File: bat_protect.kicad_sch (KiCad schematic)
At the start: 16 parts

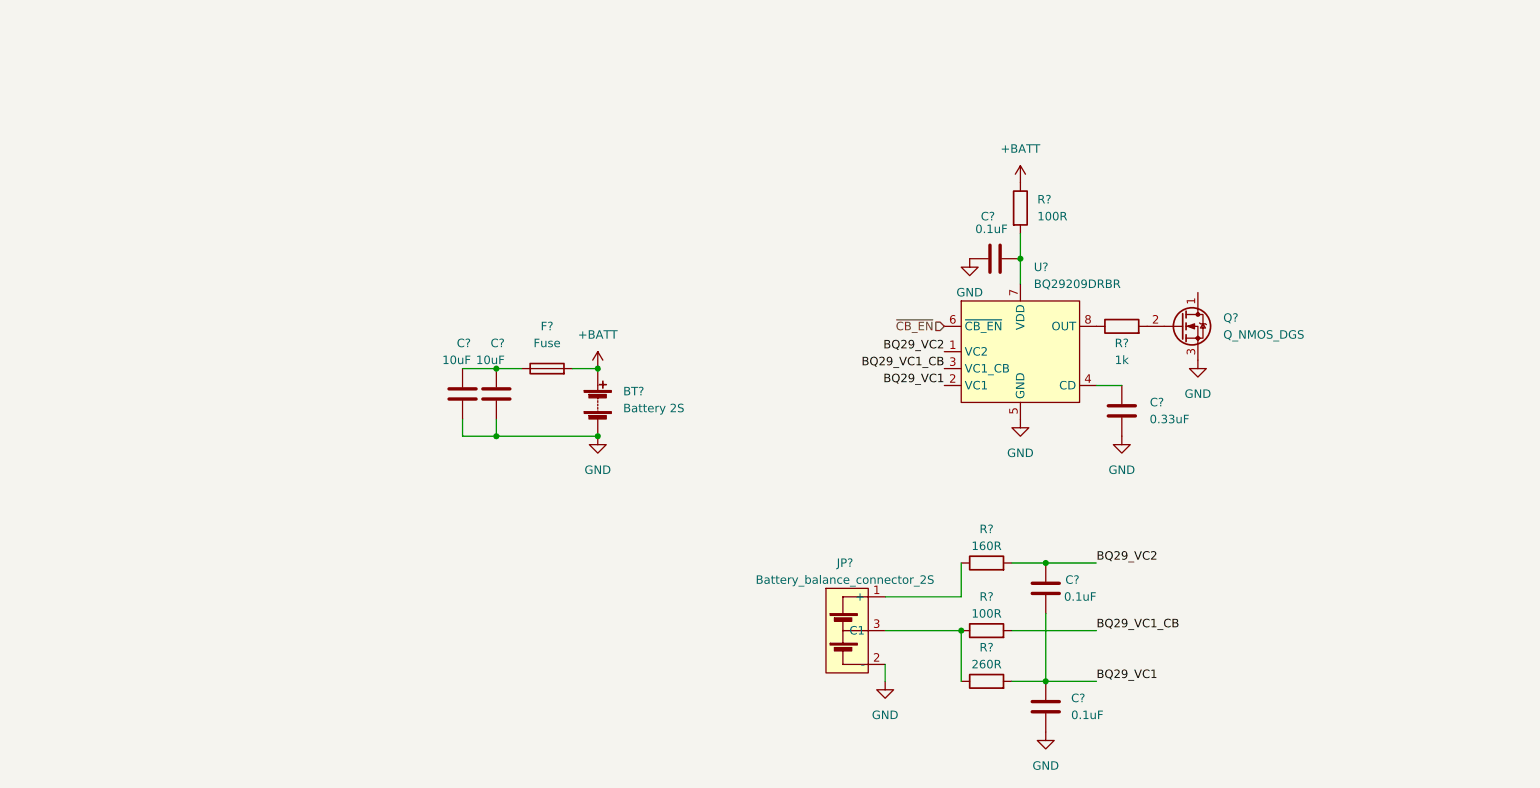
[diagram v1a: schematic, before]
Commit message: added audio ref schematic, added bat to 5V, added shift register, connected devices with other periferals
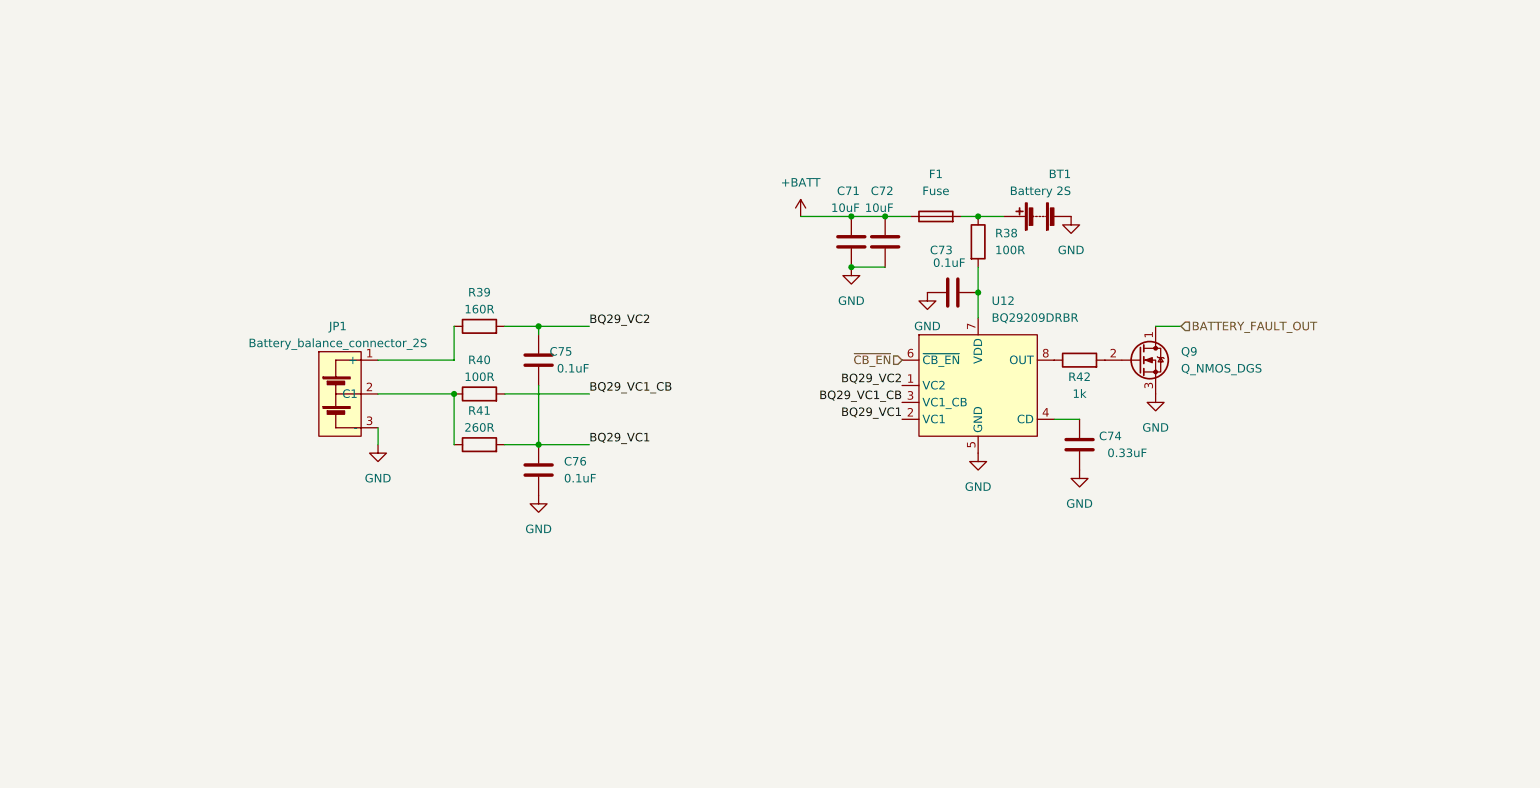
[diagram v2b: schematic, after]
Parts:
- gave numbers to parts that had none: 16
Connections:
- net +BATT: now also C71.2, C72.2, F1.1; no longer BT1.1 (+), F1.2, R38.1
- net GND: now also JP1.3 (-); no longer JP1.2 (-)
- net at R40.1, R41.1: now also JP1.2 (C1); no longer JP1.3 (C1)
- net BATTERY_FAULT_OUT: now reaches Q9.1 (D)
- new net: BT1.1 (+), F1.2, R38.1
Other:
- moved on the sheet: BT1, C71, C72, C73, C74, C75, C76, F1, JP1, Q9, R38, R39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

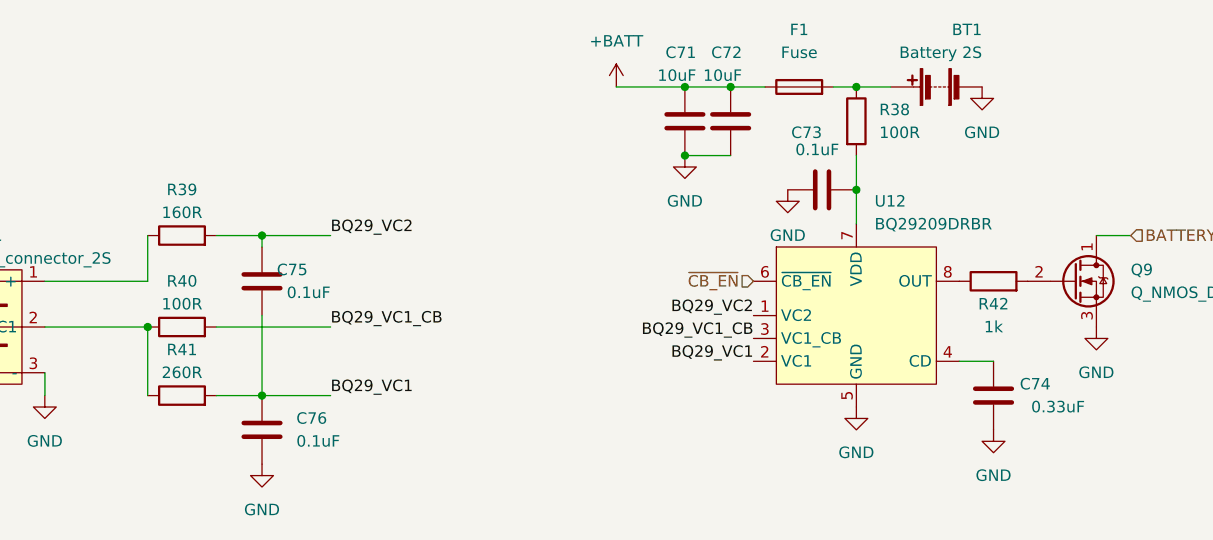
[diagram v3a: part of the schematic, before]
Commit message: minor optimized pinassignement, added capacitors, added connectors
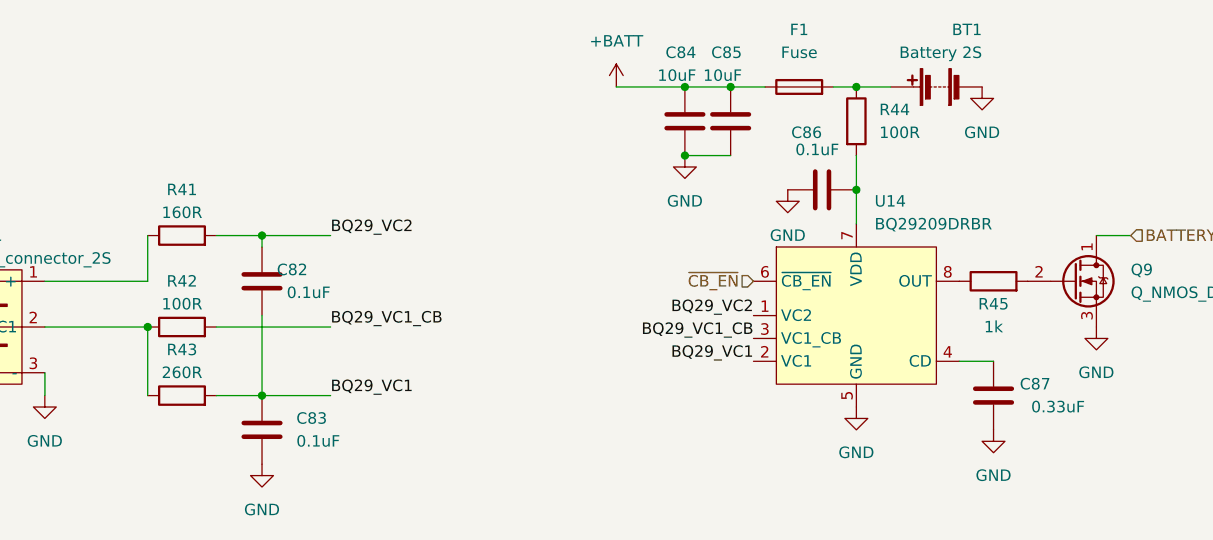
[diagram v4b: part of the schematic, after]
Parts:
- renumbered C75 to C82, C76 to C83, C71 to C84, C72 to C85, C73 to C86, C74 to C87, R39 to R41, R40 to R42, R41 to R43, R38 to R44, R42 to R45, U12 to U14
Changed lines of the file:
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@@
   (symbol (lib_id "power:GND") (at 78.74 99.06 0) (unit 1)
     (in_bom yes) (on_board yes) (fields_autoplaced)
-    (property "Reference" "#PWR0198" (id 0) (at 78.74 105.41 0)
+    (property "Reference" "#PWR0110" (id 0) (at 78.74 105.41 0)
       (effects (font (size 1.27 1.27)) hide)
     )
@@
   (symbol (lib_id "Device:R") (at 93.98 91.44 90) (unit 1)
     (in_bom yes) (on_board yes)
-    (property "Reference" "R40" (id 0) (at 93.98 86.36 90))
+    (property "Reference" "R42" (id 0) (at 93.98 86.36 90))
     (property "Value" "100R" (id 1) (at 93.98 88.9 90))
     (property "Footprint" "" (id 2) (at 93.98 93.218 90)
@@
   (symbol (lib_id "power:+BATT") (at 142.24 64.77 0) (unit 1)
     (in_bom yes) (on_board yes) (fields_autoplaced)
-    (property "Reference" "#PWR0193" (id 0) (at 142.24 68.58 0)
+    (property "Reference" "#PWR0112" (id 0) (at 142.24 68.58 0)
       (effects (font (size 1.27 1.27)) hide)
     )
@@
   (symbol (lib_id "power:GND") (at 102.87 106.68 0) (unit 1)
     (in_bom yes) (on_board yes) (fields_autoplaced)
-    (property "Reference" "#PWR0197" (id 0) (at 102.87 113.03 0)
+    (property "Reference" "#PWR0111" (id 0) (at 102.87 113.03 0)
       (effects (font (size 1.27 1.27)) hide)
     )
@@
   (symbol (lib_id "power:GND") (at 168.91 100.33 0) (unit 1)
     (in_bom yes) (on_board yes) (fields_autoplaced)
-    (property "Reference" "#PWR0191" (id 0) (at 168.91 106.68 0)
+    (property "Reference" "#PWR0115" (id 0) (at 168.91 106.68 0)
       (effects (font (size 1.27 1.27)) hide)
     )
@@
   (symbol (lib_id "power:GND") (at 149.86 72.39 0) (unit 1)
     (in_bom yes) (on_board yes) (fields_autoplaced)
-    (property "Reference" "#PWR0190" (id 0) (at 149.86 78.74 0)
+    (property "Reference" "#PWR0113" (id 0) (at 149.86 78.74 0)
       (effects (font (size 1.27 1.27)) hide)
     )
@@
   (symbol (lib_id "power:GND") (at 182.88 64.77 0) (unit 1)
     (in_bom yes) (on_board yes) (fields_autoplaced)
-    (property "Reference" "#PWR0242" (id 0) (at 182.88 71.12 0)
+    (property "Reference" "#PWR0116" (id 0) (at 182.88 71.12 0)
       (effects (font (size 1.27 1.27)) hide)
     )
@@
   (symbol (lib_id "Device:R") (at 93.98 81.28 90) (unit 1)
     (in_bom yes) (on_board yes)
-    (property "Reference" "R39" (id 0) (at 93.98 76.2 90))
+    (property "Reference" "R41" (id 0) (at 93.98 76.2 90))
     (property "Value" "160R" (id 1) (at 93.98 78.74 90))
     (property "Footprint" "" (id 2) (at 93.98 83.058 90)
@@
   (symbol (lib_id "power:GND") (at 161.29 76.2 0) (unit 1)
     (in_bom yes) (on_board yes) (fields_autoplaced)
-    (property "Reference" "#PWR0192" (id 0) (at 161.29 82.55 0)
+    (property "Reference" "#PWR0114" (id 0) (at 161.29 82.55 0)
       (effects (font (size 1.27 1.27)) hide)
     )
@@
   (symbol (lib_id "Device:C") (at 184.15 99.06 0) (mirror x) (unit 1)
     (in_bom yes) (on_board yes)
-    (property "Reference" "C74" (id 0) (at 190.5 97.79 0)
+    (property "Reference" "C87" (id 0) (at 190.5 97.79 0)
       (effects (font (size 1.27 1.27)) (justify right))
     )
@@
   (symbol (lib_id "Device:R") (at 184.15 86.36 90) (unit 1)
     (in_bom yes) (on_board yes)
-    (property "Reference" "R42" (id 0) (at 184.15 88.9 90))
+    (property "Reference" "R45" (id 0) (at 184.15 88.9 90))
     (property "Value" "1k" (id 1) (at 184.15 91.44 90))
     (property "Footprint" "" (id 2) (at 184.15 88.138 90)
@@
   (symbol (lib_id "Device:C") (at 102.87 102.87 0) (mirror y) (unit 1)
     (in_bom yes) (on_board yes)
-    (property "Reference" "C76" (id 0) (at 106.68 101.6 0)
+    (property "Reference" "C83" (id 0) (at 106.68 101.6 0)
       (effects (font (size 1.27 1.27)) (justify right))
     )
@@
   (symbol (lib_id "power:GND") (at 195.58 91.44 0) (unit 1)
     (in_bom yes) (on_board yes) (fields_autoplaced)
-    (property "Reference" "#PWR0195" (id 0) (at 195.58 97.79 0)
+    (property "Reference" "#PWR0118" (id 0) (at 195.58 97.79 0)
       (effects (font (size 1.27 1.27)) hide)
     )
@@
   (symbol (lib_id "power:GND") (at 184.15 102.87 0) (unit 1)
     (in_bom yes) (on_board yes) (fields_autoplaced)
-    (property "Reference" "#PWR0196" (id 0) (at 184.15 109.22 0)
+    (property "Reference" "#PWR0117" (id 0) (at 184.15 109.22 0)
       (effects (font (size 1.27 1.27)) hide)
     )
@@
   (symbol (lib_id "Device:C") (at 149.86 68.58 0) (mirror x) (unit 1)
     (in_bom yes) (on_board yes)
-    (property "Reference" "C71" (id 0) (at 151.13 60.96 0)
+    (property "Reference" "C84" (id 0) (at 151.13 60.96 0)
       (effects (font (size 1.27 1.27)) (justify right))
     )
@@
   (symbol (lib_id "Device:C") (at 154.94 68.58 0) (mirror x) (unit 1)
     (in_bom yes) (on_board yes)
-    (property "Reference" "C72" (id 0) (at 156.21 60.96 0)
+    (property "Reference" "C85" (id 0) (at 156.21 60.96 0)
       (effects (font (size 1.27 1.27)) (justify right))
     )
@@
   (symbol (lib_id "Device:C") (at 165.1 76.2 270) (mirror x) (unit 1)
     (in_bom yes) (on_board yes)
-    (property "Reference" "C73" (id 0) (at 165.1 69.85 90)
+    (property "Reference" "C86" (id 0) (at 165.1 69.85 90)
       (effects (font (size 1.27 1.27)) (justify right))
     )
@@
   (symbol (lib_id "Device:C") (at 102.87 86.36 0) (mirror x) (unit 1)
     (in_bom yes) (on_board yes)
-    (property "Reference" "C75" (id 0) (at 107.95 85.09 0)
+    (property "Reference" "C82" (id 0) (at 107.95 85.09 0)
       (effects (font (size 1.27 1.27)) (justify right))
     )
@@
   (symbol (lib_id "Device:R") (at 93.98 99.06 90) (unit 1)
     (in_bom yes) (on_board yes)
-    (property "Reference" "R41" (id 0) (at 93.98 93.98 90))
+    (property "Reference" "R43" (id 0) (at 93.98 93.98 90))
     (property "Value" "260R" (id 1) (at 93.98 96.52 90))
     (property "Footprint" "" (id 2) (at 93.98 100.838 90)
@@
   (symbol (lib_id "Device:R") (at 168.91 68.58 0) (unit 1)
     (in_bom yes) (on_board yes) (fields_autoplaced)
-    (property "Reference" "R38" (id 0) (at 171.45 67.3099 0)
+    (property "Reference" "R44" (id 0) (at 171.45 67.3099 0)
       (effects (font (size 1.27 1.27)) (justify left))
     )
@@
   (symbol (lib_id "airsoft_controller:BQ29209DRBR") (at 168.91 90.17 0) (unit 1)
     (in_bom yes) (on_board yes) (fields_autoplaced)
-    (property "Reference" "U12" (id 0) (at 170.9294 77.47 0)
-      (effects (font (size 1.27 1.27)) (justify left))
-    )
+    (property "Reference" "U14" (id 0) (at 170.9294 77.47 0)
+      (effects (font (size 1.27 1.27)) (justify left))
+    )

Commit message: PI LC lowpass filter, added CP2012 reset, added connectors
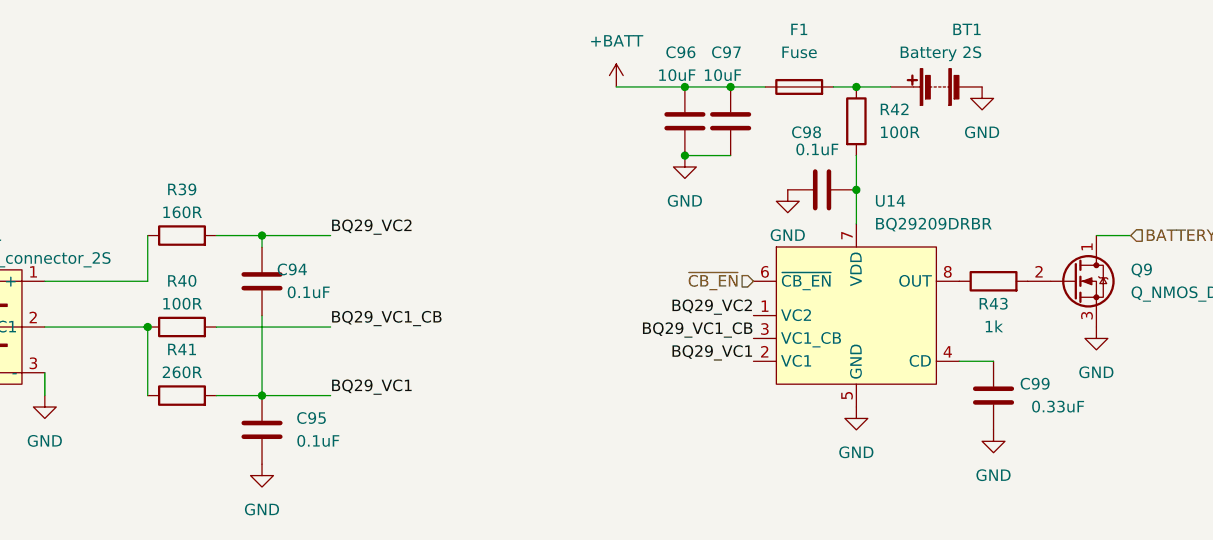
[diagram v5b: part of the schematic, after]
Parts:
- renumbered C82 to C94, C83 to C95, C84 to C96, C85 to C97, C86 to C98, C87 to C99, R41 to R39, R42 to R40, R43 to R41, R44 to R42, R45 to R43
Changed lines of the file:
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@@
   (symbol (lib_id "power:GND") (at 78.74 99.06 0) (unit 1)
     (in_bom yes) (on_board yes) (fields_autoplaced)
-    (property "Reference" "#PWR0110" (id 0) (at 78.74 105.41 0)
+    (property "Reference" "#PWR0117" (id 0) (at 78.74 105.41 0)
       (effects (font (size 1.27 1.27)) hide)
     )
@@
   (symbol (lib_id "Device:R") (at 93.98 91.44 90) (unit 1)
     (in_bom yes) (on_board yes)
-    (property "Reference" "R42" (id 0) (at 93.98 86.36 90))
+    (property "Reference" "R40" (id 0) (at 93.98 86.36 90))
     (property "Value" "100R" (id 1) (at 93.98 88.9 90))
     (property "Footprint" "" (id 2) (at 93.98 93.218 90)
@@
   (symbol (lib_id "power:+BATT") (at 142.24 64.77 0) (unit 1)
     (in_bom yes) (on_board yes) (fields_autoplaced)
-    (property "Reference" "#PWR0112" (id 0) (at 142.24 68.58 0)
+    (property "Reference" "#PWR0119" (id 0) (at 142.24 68.58 0)
       (effects (font (size 1.27 1.27)) hide)
     )
@@
   (symbol (lib_id "power:GND") (at 102.87 106.68 0) (unit 1)
     (in_bom yes) (on_board yes) (fields_autoplaced)
-    (property "Reference" "#PWR0111" (id 0) (at 102.87 113.03 0)
+    (property "Reference" "#PWR0118" (id 0) (at 102.87 113.03 0)
       (effects (font (size 1.27 1.27)) hide)
     )
@@
   (symbol (lib_id "power:GND") (at 168.91 100.33 0) (unit 1)
     (in_bom yes) (on_board yes) (fields_autoplaced)
-    (property "Reference" "#PWR0115" (id 0) (at 168.91 106.68 0)
+    (property "Reference" "#PWR0122" (id 0) (at 168.91 106.68 0)
       (effects (font (size 1.27 1.27)) hide)
     )
@@
   (symbol (lib_id "power:GND") (at 149.86 72.39 0) (unit 1)
     (in_bom yes) (on_board yes) (fields_autoplaced)
-    (property "Reference" "#PWR0113" (id 0) (at 149.86 78.74 0)
+    (property "Reference" "#PWR0120" (id 0) (at 149.86 78.74 0)
       (effects (font (size 1.27 1.27)) hide)
     )
@@
   (symbol (lib_id "power:GND") (at 182.88 64.77 0) (unit 1)
     (in_bom yes) (on_board yes) (fields_autoplaced)
-    (property "Reference" "#PWR0116" (id 0) (at 182.88 71.12 0)
+    (property "Reference" "#PWR0123" (id 0) (at 182.88 71.12 0)
       (effects (font (size 1.27 1.27)) hide)
     )
@@
   (symbol (lib_id "Device:R") (at 93.98 81.28 90) (unit 1)
     (in_bom yes) (on_board yes)
-    (property "Reference" "R41" (id 0) (at 93.98 76.2 90))
+    (property "Reference" "R39" (id 0) (at 93.98 76.2 90))
     (property "Value" "160R" (id 1) (at 93.98 78.74 90))
     (property "Footprint" "" (id 2) (at 93.98 83.058 90)
@@
   (symbol (lib_id "power:GND") (at 161.29 76.2 0) (unit 1)
     (in_bom yes) (on_board yes) (fields_autoplaced)
-    (property "Reference" "#PWR0114" (id 0) (at 161.29 82.55 0)
+    (property "Reference" "#PWR0121" (id 0) (at 161.29 82.55 0)
       (effects (font (size 1.27 1.27)) hide)
     )
@@
   (symbol (lib_id "Device:C") (at 184.15 99.06 0) (mirror x) (unit 1)
     (in_bom yes) (on_board yes)
-    (property "Reference" "C87" (id 0) (at 190.5 97.79 0)
+    (property "Reference" "C99" (id 0) (at 190.5 97.79 0)
       (effects (font (size 1.27 1.27)) (justify right))
     )
@@
   (symbol (lib_id "Device:R") (at 184.15 86.36 90) (unit 1)
     (in_bom yes) (on_board yes)
-    (property "Reference" "R45" (id 0) (at 184.15 88.9 90))
+    (property "Reference" "R43" (id 0) (at 184.15 88.9 90))
     (property "Value" "1k" (id 1) (at 184.15 91.44 90))
     (property "Footprint" "" (id 2) (at 184.15 88.138 90)
@@
   (symbol (lib_id "Device:C") (at 102.87 102.87 0) (mirror y) (unit 1)
     (in_bom yes) (on_board yes)
-    (property "Reference" "C83" (id 0) (at 106.68 101.6 0)
+    (property "Reference" "C95" (id 0) (at 106.68 101.6 0)
       (effects (font (size 1.27 1.27)) (justify right))
     )
@@
   (symbol (lib_id "power:GND") (at 195.58 91.44 0) (unit 1)
     (in_bom yes) (on_board yes) (fields_autoplaced)
-    (property "Reference" "#PWR0118" (id 0) (at 195.58 97.79 0)
+    (property "Reference" "#PWR0125" (id 0) (at 195.58 97.79 0)
       (effects (font (size 1.27 1.27)) hide)
     )
@@
   (symbol (lib_id "power:GND") (at 184.15 102.87 0) (unit 1)
     (in_bom yes) (on_board yes) (fields_autoplaced)
-    (property "Reference" "#PWR0117" (id 0) (at 184.15 109.22 0)
+    (property "Reference" "#PWR0124" (id 0) (at 184.15 109.22 0)
       (effects (font (size 1.27 1.27)) hide)
     )
@@
   (symbol (lib_id "Device:C") (at 149.86 68.58 0) (mirror x) (unit 1)
     (in_bom yes) (on_board yes)
-    (property "Reference" "C84" (id 0) (at 151.13 60.96 0)
+    (property "Reference" "C96" (id 0) (at 151.13 60.96 0)
       (effects (font (size 1.27 1.27)) (justify right))
     )
@@
   (symbol (lib_id "Device:C") (at 154.94 68.58 0) (mirror x) (unit 1)
     (in_bom yes) (on_board yes)
-    (property "Reference" "C85" (id 0) (at 156.21 60.96 0)
+    (property "Reference" "C97" (id 0) (at 156.21 60.96 0)
       (effects (font (size 1.27 1.27)) (justify right))
     )
@@
   (symbol (lib_id "Device:C") (at 165.1 76.2 270) (mirror x) (unit 1)
     (in_bom yes) (on_board yes)
-    (property "Reference" "C86" (id 0) (at 165.1 69.85 90)
+    (property "Reference" "C98" (id 0) (at 165.1 69.85 90)
       (effects (font (size 1.27 1.27)) (justify right))
     )
@@
   (symbol (lib_id "Device:C") (at 102.87 86.36 0) (mirror x) (unit 1)
     (in_bom yes) (on_board yes)
-    (property "Reference" "C82" (id 0) (at 107.95 85.09 0)
+    (property "Reference" "C94" (id 0) (at 107.95 85.09 0)
       (effects (font (size 1.27 1.27)) (justify right))
     )
@@
   (symbol (lib_id "Device:R") (at 93.98 99.06 90) (unit 1)
     (in_bom yes) (on_board yes)
-    (property "Reference" "R43" (id 0) (at 93.98 93.98 90))
+    (property "Reference" "R41" (id 0) (at 93.98 93.98 90))
     (property "Value" "260R" (id 1) (at 93.98 96.52 90))
     (property "Footprint" "" (id 2) (at 93.98 100.838 90)
@@
   (symbol (lib_id "Device:R") (at 168.91 68.58 0) (unit 1)
     (in_bom yes) (on_board yes) (fields_autoplaced)
-    (property "Reference" "R44" (id 0) (at 171.45 67.3099 0)
-      (effects (font (size 1.27 1.27)) (justify left))
-    )
+    (property "Reference" "R42" (id 0) (at 171.45 67.3099 0)
+      (effects (font (size 1.27 1.27)) (justify left))
+    )
